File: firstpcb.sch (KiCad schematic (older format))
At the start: 10 parts

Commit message: shematic
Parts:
- added C? (x2): 22pF, symbol Device:C_Small
- added R?: 10k, symbol Device:R_Small
- added SW?: SW_Push, symbol Switch:SW_Push
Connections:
- net +5V: now also R?.1
- net GND: now also Y?.2, Y?.4, C?.2, C?.2, SW?.1
- net at U?.13 (~RESET): now also R?.2, SW?.2
- net at U?.16 (XTAL2), Y?.3: now also C?.1
- net at U?.17 (XTAL1), Y?.1: now also C?.1
- net D-: now reaches R?.2
- net D+: now reaches R?.2
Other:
- moved on the sheet: C?, R?

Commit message: schematic
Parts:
- added D? (x4): SOD-123, symbol Device:D_Small
- added F?: 500mA, symbol Device:Polyfuse
- added MX? (x4): MX-NoLED, symbol MX_Alps_Hybrid:MX-NoLED
- added USB?: Molex-0548190589, symbol random-keyboard-parts:Molex-0548190589
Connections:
- net +5V: now also F?.1
- net D+: now also USB?.5 (VBUS)
- net D-: now also USB?.4 (D-)
- net GND: now also USB?.1 (GND)
- new net: D?.2 (A), MX?.2 (ROW) (x4)
- new net COL0: MX?.1 (COL), MX?.1 (COL)
- new net COL1: MX?.1 (COL), MX?.1 (COL)
- new net ROW0: D?.1 (K), D?.1 (K)
- new net ROW1: D?.1 (K), D?.1 (K)
- new net VCC: F?.2, USB?.6 (SHIELD)
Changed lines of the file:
@@
 Wire Wire Line
 	2700 3000 2250 3000
+$Comp
+L random-keyboard-parts:Molex-0548190589 USB?
+U 1 1 636BF531
+P 6750 2050
+F 0 "USB?" V 7287 2017 60  0000 C CNN
+F 1 "Molex-0548190589" V 7181 2017 60  0000 C CNN
+F 2 "" H 6750 2050 60  0001 C CNN
+F 3 "" H 6750 2050 60  0001 C CNN
+	1    6750 2050
+	0    -1   -1   0
+$EndComp
+$Comp
+L power:VCC #PWR?
+U 1 1 636C0166
+P 7350 1750
+F 0 "#PWR?" H 7350 1600 50  0001 C CNN
+F 1 "VCC" H 7367 1923 50  0000 C CNN
+F 2 "" H 7350 1750 50  0001 C CNN
+F 3 "" H 7350 1750 50  0001 C CNN
+	1    7350 1750
+	1    0    0    -1
+$EndComp
+$Comp
+L Device:Polyfuse F?
+U 1 1 636C3A9A
+P 7700 1750
+F 0 "F?" V 7475 1750 50  0000 C CNN
+F 1 "500mA" V 7566 1750 50  0000 C CNN
+F 2 "" H 7750 1550 50  0001 L CNN
+F 3 "~" H 7700 1750 50  0001 C CNN
+	1    7700 1750
+	0    1    1    0
+$EndComp
+$Comp
+L power:+5V #PWR?
+U 1 1 636C5D2B
+P 8100 1750
+F 0 "#PWR?" H 8100 1600 50  0001 C CNN
+F 1 "+5V" H 8115 1923 50  0000 C CNN
+F 2 "" H 8100 1750 50  0001 C CNN
+F 3 "" H 8100 1750 50  0001 C CNN
+	1    8100 1750
+	1    0    0    -1
+$EndComp
+Wire Wire Line
+	7050 1750 7350 1750
+Wire Wire Line
+	7850 1750 8100 1750
+Connection ~ 7350 1750
+Wire Wire Line
+	7350 1750 7550 1750
+$Comp
+L power:GND #PWR?
+U 1 1 636C745E
+P 7150 2250
+F 0 "#PWR?" H 7150 2000 50  0001 C CNN
+F 1 "GND" H 7155 2077 50  0000 C CNN
+F 2 "" H 7150 2250 50  0001 C CNN
+F 3 "" H 7150 2250 50  0001 C CNN
+	1    7150 2250
+	1    0    0    -1
+$EndComp
+Text GLabel 7050 1950 2    50   Input ~ 0
+D-
+Text GLabel 7050 1850 2    50   Input ~ 0
+D+
+Wire Wire Line
+	7050 2250 7150 2250
+$Comp
+L MX_Alps_Hybrid:MX-NoLED MX?
+U 1 1 636E001D
+P 7250 3300
+F 0 "MX?" H 7283 3523 60  0000 C CNN
+F 1 "MX-NoLED" H 7283 3449 20  0000 C CNN
+F 2 "" H 6625 3275 60  0001 C CNN
+F 3 "" H 6625 3275 60  0001 C CNN
+	1    7250 3300
+	1    0    0    -1
+$EndComp
+$Comp
+L Device:D_Small D?
+U 1 1 636EA45A
+P 7100 3600
+F 0 "D?" V 7146 3532 50  0000 R CNN
+F 1 "SOD-123" V 7055 3532 50  0000 R CNN
+F 2 "" V 7100 3600 50  0001 C CNN
+F 3 "~" V 7100 3600 50  0001 C CNN
+	1    7100 3600
+	0    -1   -1   0
+$EndComp
+Wire Wire Line
+	7200 3450 7100 3450
+Wire Wire Line
+	7100 3450 7100 3500
+$Comp
+L MX_Alps_Hybrid:MX-NoLED MX?
+U 1 1 636F0FB9
+P 7800 3300
+F 0 "MX?" H 7833 3523 60  0000 C CNN
+F 1 "MX-NoLED" H 7833 3449 20  0000 C CNN
+F 2 "" H 7175 3275 60  0001 C CNN
+F 3 "" H 7175 3275 60  0001 C CNN
+	1    7800 3300
+	1    0    0    -1
+$EndComp
+$Comp
+L Device:D_Small D?
+U 1 1 636F0FBF
+P 7650 3600
+F 0 "D?" V 7696 3532 50  0000 R CNN
+F 1 "SOD-123" V 7605 3532 50  0000 R CNN
+F 2 "" V 7650 3600 50  0001 C CNN
+F 3 "~" V 7650 3600 50  0001 C CNN
+	1    7650 3600
+	0    -1   -1   0
+$EndComp
+Wire Wire Line
+	7750 3450 7650 3450
+Wire Wire Line
+	7650 3450 7650 3500
+$Comp
+L MX_Alps_Hybrid:MX-NoLED MX?
+U 1 1 636F86FE
+P 7250 4000
+F 0 "MX?" H 7283 4223 60  0000 C CNN
+F 1 "MX-NoLED" H 7283 4149 20  0000 C CNN
+F 2 "" H 6625 3975 60  0001 C CNN
+F 3 "" H 6625 3975 60  0001 C CNN
+	1    7250 4000
+	1    0    0    -1
+$EndComp
+$Comp
+L Device:D_Small D?
+U 1 1 636F8704
+P 7100 4300
+F 0 "D?" V 7146 4232 50  0000 R CNN
+F 1 "SOD-123" V 7055 4232 50  0000 R CNN
+F 2 "" V 7100 4300 50  0001 C CNN
+F 3 "~" V 7100 4300 50  0001 C CNN
+	1    7100 4300
+	0    -1   -1   0
+$EndComp
+Wire Wire Line
+	7200 4150 7100 4150
+Wire Wire Line
+	7100 4150 7100 4200
+$Comp
+L MX_Alps_Hybrid:MX-NoLED MX?
+U 1 1 636F870C
+P 7800 4000
+F 0 "MX?" H 7833 4223 60  0000 C CNN
+F 1 "MX-NoLED" H 7833 4149 20  0000 C CNN
+F 2 "" H 7175 3975 60  0001 C CNN
+F 3 "" H 7175 3975 60  0001 C CNN
+	1    7800 4000
+	1    0    0    -1
+$EndComp
+$Comp
+L Device:D_Small D?
+U 1 1 636F8712
+P 7650 4300
+F 0 "D?" V 7696 4232 50  0000 R CNN
+F 1 "SOD-123" V 7605 4232 50  0000 R CNN
+F 2 "" V 7650 4300 50  0001 C CNN
+F 3 "~" V 7650 4300 50  0001 C CNN
+	1    7650 4300
+	0    -1   -1   0
+$EndComp
+Wire Wire Line
+	7750 4150 7650 4150
+Wire Wire Line
+	7650 4150 7650 4200
+Wire Wire Line
+	7950 2900 7950 3250
+Connection ~ 7950 3250
+Wire Wire Line
+	7950 3250 7950 3950
+Wire Wire Line
+	7400 2900 7400 3250
+Connection ~ 7400 3250
+Wire Wire Line
+	7400 3250 7400 3950
+Wire Wire Line
+	6850 3700 7100 3700
+Connection ~ 7100 3700
+Wire Wire Line
+	7100 3700 7650 3700
+Wire Wire Line
+	6850 4400 7100 4400
+Connection ~ 7100 4400
+Wire Wire Line
+	7100 4400 7650 4400
+Text GLabel 7400 2900 1    50   Input ~ 0
+COL0
+Text GLabel 7950 2900 1    50   Input ~ 0
+COL1
+Text GLabel 6850 3700 0    50   Input ~ 0
+ROW0
+Text GLabel 6850 4400 0    50   Input ~ 0
+ROW1
 $EndSCHEMATC

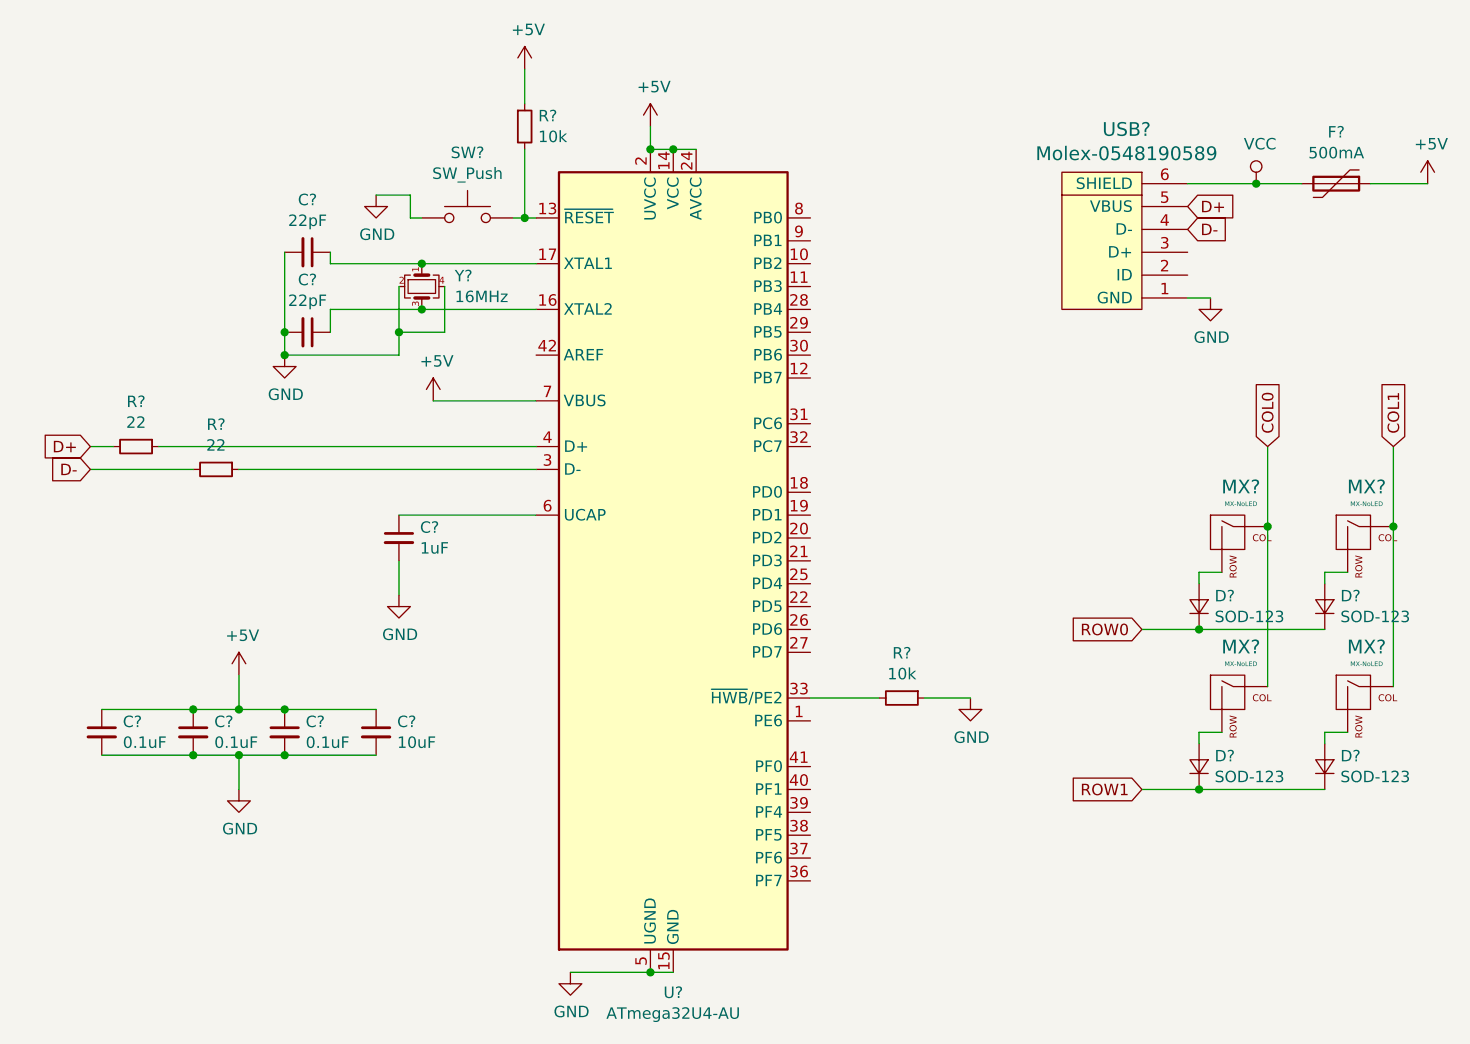
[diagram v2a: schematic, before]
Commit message: 分配封裝
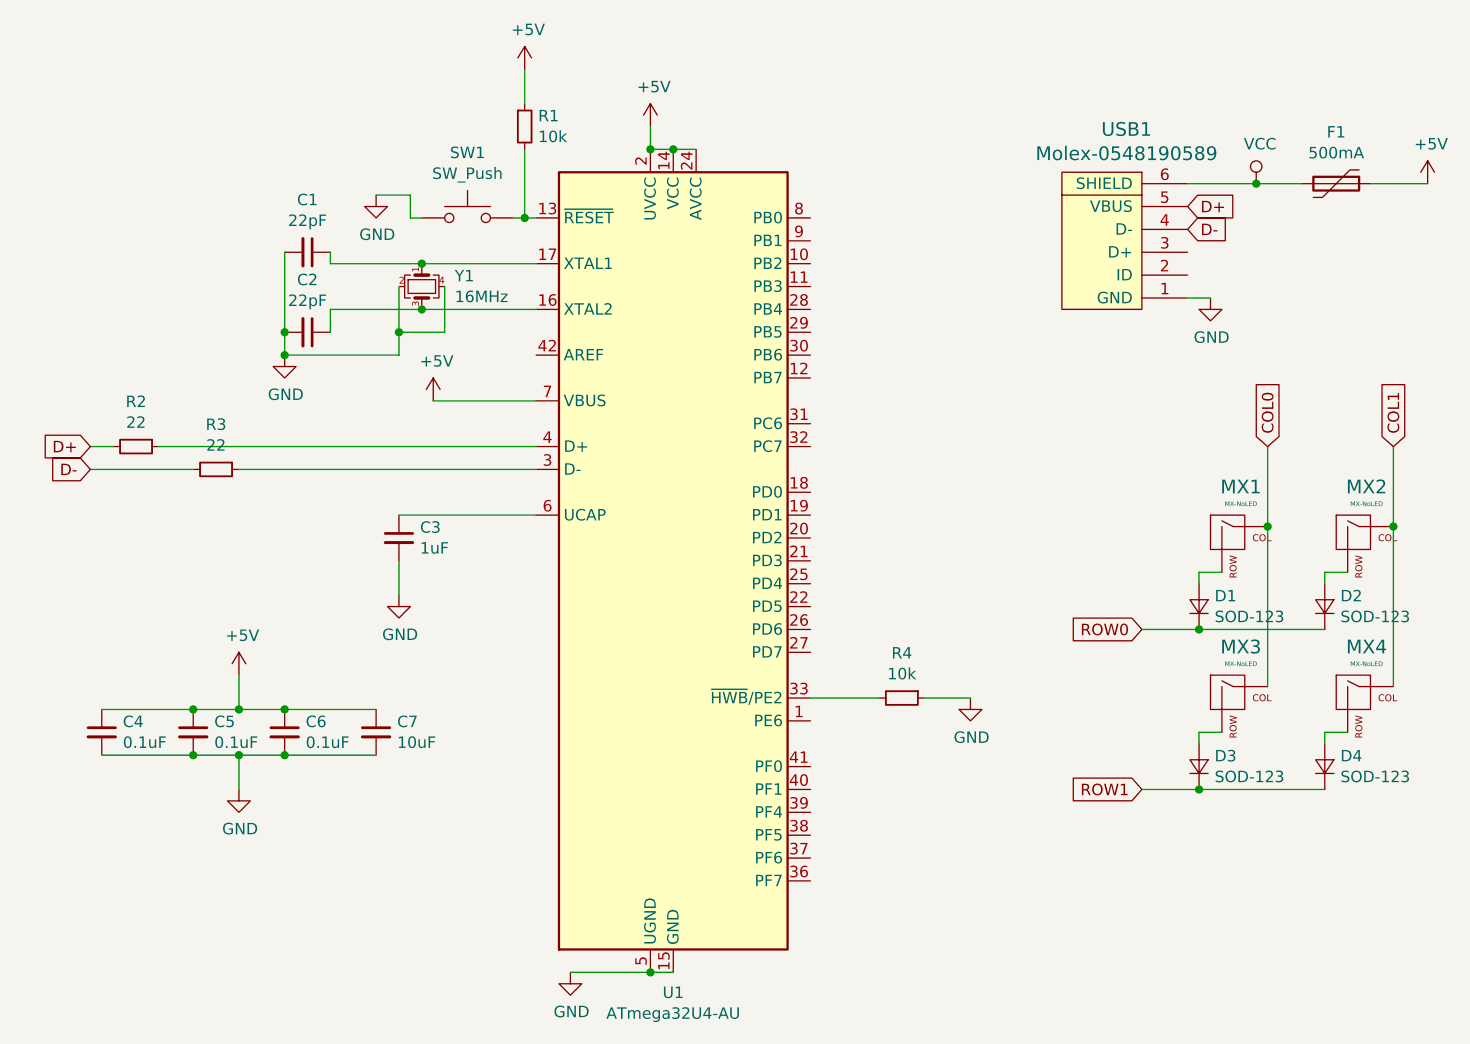
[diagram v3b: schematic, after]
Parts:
- C1, C2, C3, C4, C5, C6, C7: renamed from C?; footprint (none) -> Capacitor_SMD:C_0805_2012Metric
- D1, D2, D3, D4: renamed from D?; footprint (none) -> Diode_SMD:D_SOD-123
- F1: renamed from F?; footprint (none) -> Fuse:Fuse_1206_3216Metric
- MX1, MX2, MX3, MX4: renamed from MX?; footprint (none) -> MX_Only:MXOnly-1U
- R1, R2, R3, R4: renamed from R?; footprint (none) -> Resistor_SMD:R_0805_2012Metric
- Y1: renamed from Y?; footprint (none) -> Crystal:Crystal_SMD_3225-4Pin_3.2x2.5mm
- gave numbers to parts that had none: 3

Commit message: footprint
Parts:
- SW1: footprint (none) -> random-keyboard-parts:SKQG-1155865
- USB1: footprint (none) -> random-keyboard-parts:Molex-0548190589
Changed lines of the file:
@@
 F 0 "SW1" H 3900 2185 50  0000 C CNN
 F 1 "SW_Push" H 3900 2094 50  0000 C CNN
-F 2 "" H 3900 2100 50  0001 C CNN
+F 2 "random-keyboard-parts:SKQG-1155865" H 3900 2100 50  0001 C CNN
 F 3 "~" H 3900 2100 50  0001 C CNN
 	1    3900 1900
@@
 F 0 "USB1" V 7287 2017 60  0000 C CNN
 F 1 "Molex-0548190589" V 7181 2017 60  0000 C CNN
-F 2 "" H 6750 2050 60  0001 C CNN
+F 2 "random-keyboard-parts:Molex-0548190589" H 6750 2050 60  0001 C CNN
 F 3 "" H 6750 2050 60  0001 C CNN
 	1    6750 2050

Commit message: 0
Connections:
- net COL0: now also U1.28 (PB4)
- net COL1: now also U1.29 (PB5)
- net D+: now also USB1.3 (D+); no longer USB1.5 (VBUS)
- net ROW0: now also U1.27 (PD7)
- net ROW1: now also U1.30 (PB6)
- net VCC: now also USB1.5 (VBUS); no longer USB1.6 (SHIELD)
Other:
- moved on the sheet: F1
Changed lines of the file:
@@
 L power:VCC #PWR0111
 U 1 1 636C0166
-P 7350 1750
-F 0 "#PWR0111" H 7350 1600 50  0001 C CNN
-F 1 "VCC" H 7367 1923 50  0000 C CNN
-F 2 "" H 7350 1750 50  0001 C CNN
-F 3 "" H 7350 1750 50  0001 C CNN
-	1    7350 1750
+P 7350 1850
+F 0 "#PWR0111" H 7350 1700 50  0001 C CNN
+F 1 "VCC" H 7367 2023 50  0000 C CNN
+F 2 "" H 7350 1850 50  0001 C CNN
+F 3 "" H 7350 1850 50  0001 C CNN
+	1    7350 1850
 	1    0    0    -1
 $EndComp
@@
 L Device:Polyfuse F1
 U 1 1 636C3A9A
-P 7700 1750
-F 0 "F1" V 7475 1750 50  0000 C CNN
-F 1 "500mA" V 7566 1750 50  0000 C CNN
-F 2 "Fuse:Fuse_1206_3216Metric" H 7750 1550 50  0001 L CNN
-F 3 "~" H 7700 1750 50  0001 C CNN
-	1    7700 1750
+P 7700 1850
+F 0 "F1" V 7475 1850 50  0000 C CNN
+F 1 "500mA" V 7566 1850 50  0000 C CNN
+F 2 "Fuse:Fuse_1206_3216Metric" H 7750 1650 50  0001 L CNN
+F 3 "~" H 7700 1850 50  0001 C CNN
+	1    7700 1850
 	0    1    1    0
 $EndComp
@@
 L power:+5V #PWR0112
 U 1 1 636C5D2B
-P 8100 1750
-F 0 "#PWR0112" H 8100 1600 50  0001 C CNN
-F 1 "+5V" H 8115 1923 50  0000 C CNN
-F 2 "" H 8100 1750 50  0001 C CNN
-F 3 "" H 8100 1750 50  0001 C CNN
-	1    8100 1750
+P 8100 1850
+F 0 "#PWR0112" H 8100 1700 50  0001 C CNN
+F 1 "+5V" H 8115 2023 50  0000 C CNN
+F 2 "" H 8100 1850 50  0001 C CNN
+F 3 "" H 8100 1850 50  0001 C CNN
+	1    8100 1850
 	1    0    0    -1
 $EndComp
 Wire Wire Line
-	7050 1750 7350 1750
+	7050 1850 7350 1850
 Wire Wire Line
-	7850 1750 8100 1750
-Connection ~ 7350 1750
+	7850 1850 8100 1850
+Connection ~ 7350 1850
 Wire Wire Line
-	7350 1750 7550 1750
+	7350 1850 7550 1850
 $Comp
 L power:GND #PWR0113
@@
 	1    0    0    -1
 $EndComp
+Text GLabel 7050 2050 2    50   Input ~ 0
+D+
 Text GLabel 7050 1950 2    50   Input ~ 0
 D-
-Text GLabel 7050 1850 2    50   Input ~ 0
-D+
 Wire Wire Line
 	7050 2250 7150 2250
@@
 Text GLabel 6850 4400 0    50   Input ~ 0
 ROW1
+Text GLabel 5400 2400 2    50   Input ~ 0
+COL1
+Text GLabel 5400 2300 2    50   Input ~ 0
+COL0
+Text GLabel 5400 3800 2    50   Input ~ 0
+ROW0
+Text GLabel 5400 2500 2    50   Input ~ 0
+ROW1
 $EndSCHEMATC
